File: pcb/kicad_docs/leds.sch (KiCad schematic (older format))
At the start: 13 parts, among them U6 74HC595

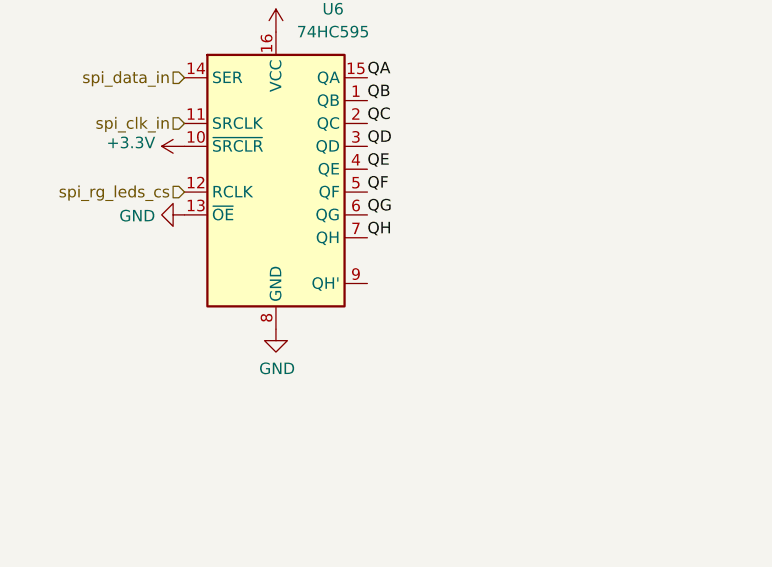
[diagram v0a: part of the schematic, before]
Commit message: add title blocks, fix some erc violations
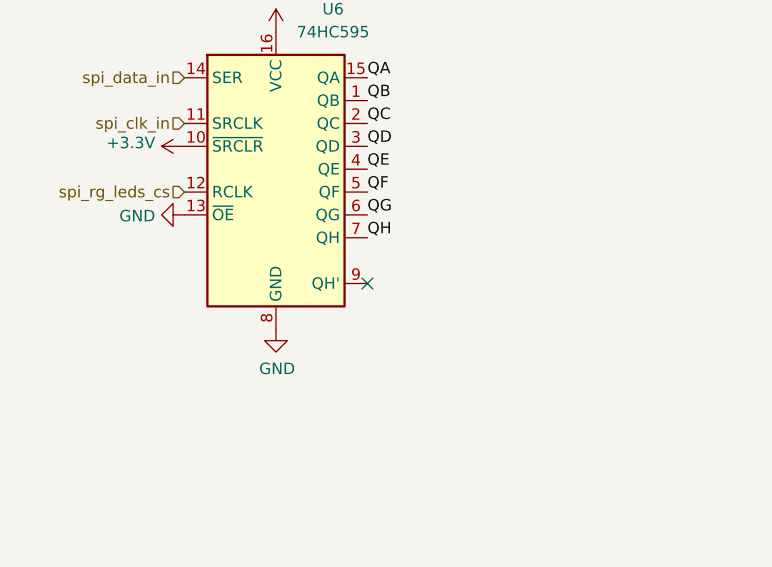
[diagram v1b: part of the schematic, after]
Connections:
- no-connect marks 0 -> 1
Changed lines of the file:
@@
 encoding utf-8
 Sheet 10 10
-Title ""
-Date ""
-Rev ""
+Title "Quad ADSR"
+Date "2020-07-31"
+Rev "0"
 Comp ""
-Comment1 ""
-Comment2 ""
-Comment3 ""
+Comment1 "creativecommons.org/licenses/by/4.0/"
+Comment2 "License: CC by 4.0"
+Comment3 "Author: Jordan Aceto"
 Comment4 ""
 $EndDescr
@@
 Text Label 5650 1450 2    50   ~ 0
 QH
+NoConn ~ 3550 2800
 $EndSCHEMATC

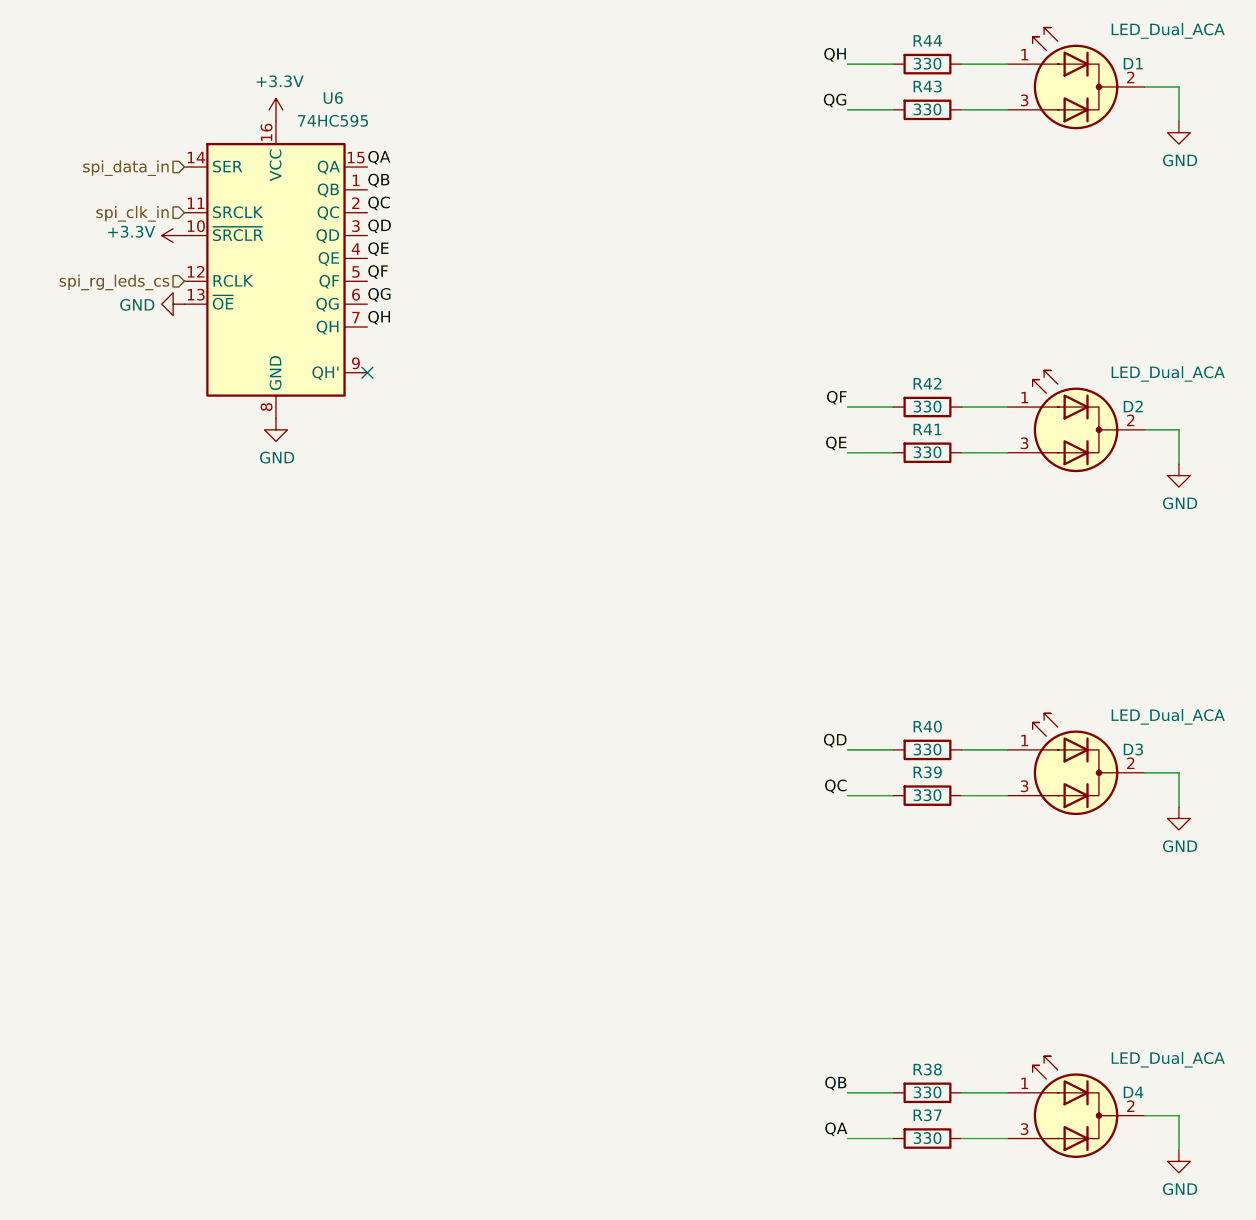
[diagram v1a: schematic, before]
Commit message: change LED current limiting resistors
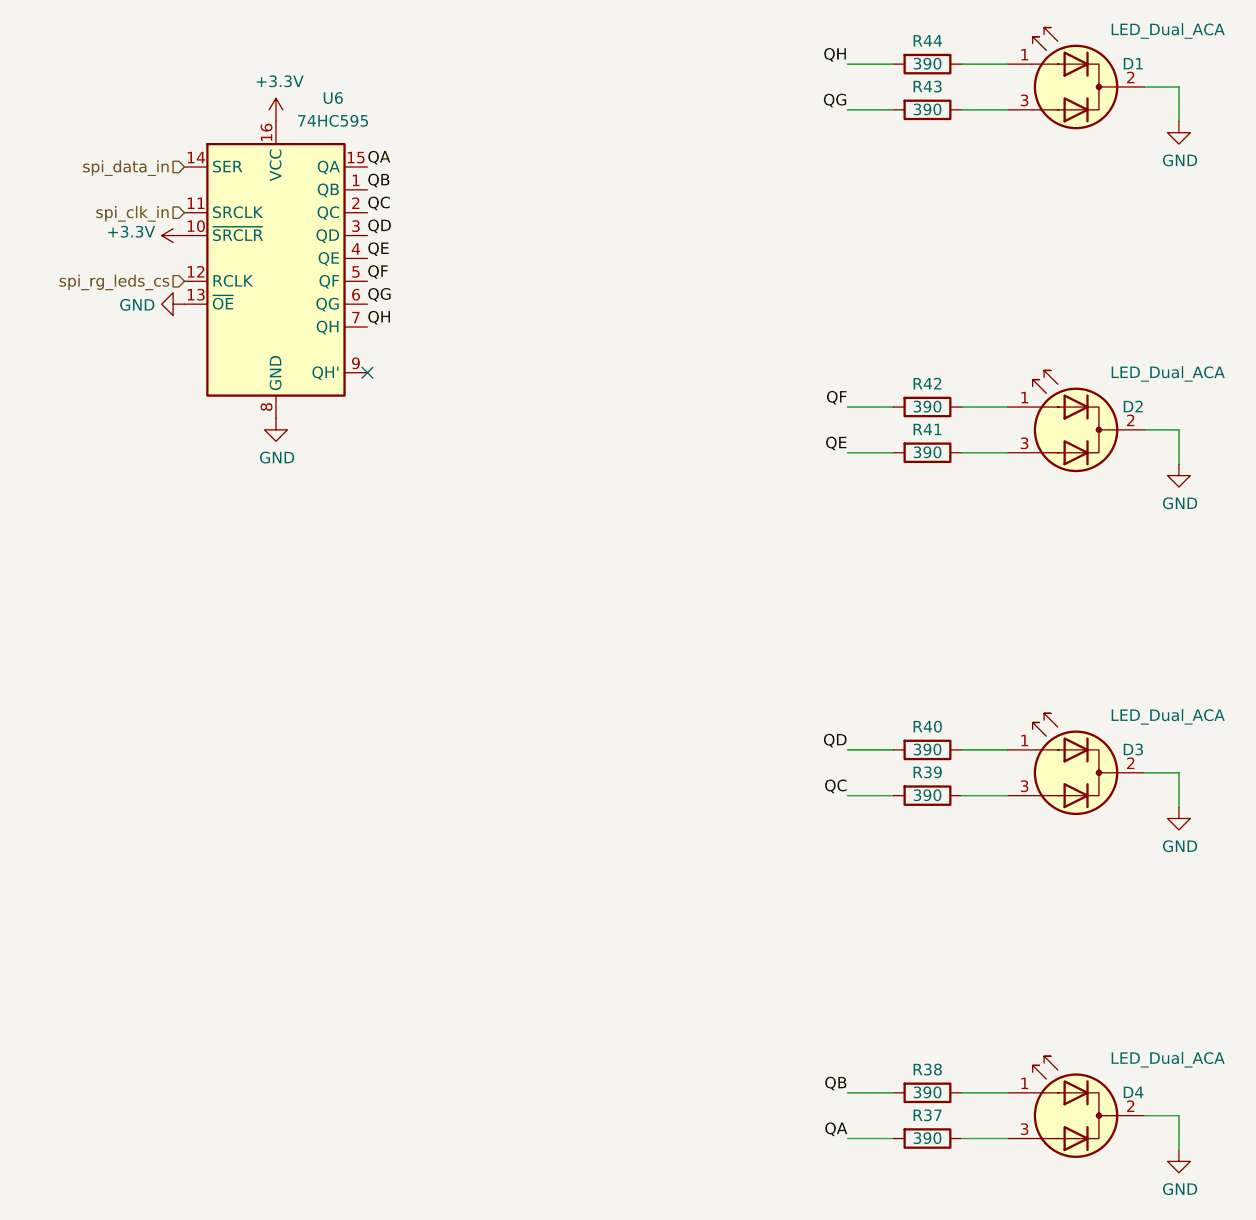
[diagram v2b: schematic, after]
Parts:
- R37, R38, R39, R40, R41, R42, R43, R44: value 330 -> 390
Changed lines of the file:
@@
 P 6000 6150
 F 0 "R37" V 5900 6150 50  0000 C CNN
-F 1 "330" V 6000 6150 50  0000 C CNN
+F 1 "390" V 6000 6150 50  0000 C CNN
 F 2 "Resistor_SMD:R_0603_1608Metric" V 5930 6150 50  0001 C CNN
 F 3 "~" H 6000 6150 50  0001 C CNN
@@
 P 6000 5950
 F 0 "R38" V 5900 5950 50  0000 C CNN
-F 1 "330" V 6000 5950 50  0000 C CNN
+F 1 "390" V 6000 5950 50  0000 C CNN
 F 2 "Resistor_SMD:R_0603_1608Metric" V 5930 5950 50  0001 C CNN
 F 3 "~" H 6000 5950 50  0001 C CNN
@@
 P 6000 4650
 F 0 "R39" V 5900 4650 50  0000 C CNN
-F 1 "330" V 6000 4650 50  0000 C CNN
+F 1 "390" V 6000 4650 50  0000 C CNN
 F 2 "Resistor_SMD:R_0603_1608Metric" V 5930 4650 50  0001 C CNN
 F 3 "~" H 6000 4650 50  0001 C CNN
@@
 P 6000 4450
 F 0 "R40" V 5900 4450 50  0000 C CNN
-F 1 "330" V 6000 4450 50  0000 C CNN
+F 1 "390" V 6000 4450 50  0000 C CNN
 F 2 "Resistor_SMD:R_0603_1608Metric" V 5930 4450 50  0001 C CNN
 F 3 "~" H 6000 4450 50  0001 C CNN
@@
 P 6000 3150
 F 0 "R41" V 5900 3150 50  0000 C CNN
-F 1 "330" V 6000 3150 50  0000 C CNN
+F 1 "390" V 6000 3150 50  0000 C CNN
 F 2 "Resistor_SMD:R_0603_1608Metric" V 5930 3150 50  0001 C CNN
 F 3 "~" H 6000 3150 50  0001 C CNN
@@
 P 6000 2950
 F 0 "R42" V 5900 2950 50  0000 C CNN
-F 1 "330" V 6000 2950 50  0000 C CNN
+F 1 "390" V 6000 2950 50  0000 C CNN
 F 2 "Resistor_SMD:R_0603_1608Metric" V 5930 2950 50  0001 C CNN
 F 3 "~" H 6000 2950 50  0001 C CNN
@@
 P 6000 1650
 F 0 "R43" V 5900 1650 50  0000 C CNN
-F 1 "330" V 6000 1650 50  0000 C CNN
+F 1 "390" V 6000 1650 50  0000 C CNN
 F 2 "Resistor_SMD:R_0603_1608Metric" V 5930 1650 50  0001 C CNN
 F 3 "~" H 6000 1650 50  0001 C CNN
@@
 P 6000 1450
 F 0 "R44" V 5900 1450 50  0000 C CNN
-F 1 "330" V 6000 1450 50  0000 C CNN
+F 1 "390" V 6000 1450 50  0000 C CNN
 F 2 "Resistor_SMD:R_0603_1608Metric" V 5930 1450 50  0001 C CNN
 F 3 "~" H 6000 1450 50  0001 C CNN
